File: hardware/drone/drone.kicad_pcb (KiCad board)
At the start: 4 copper layers, 70 parts, among them IC101 TPS63000IDRCRQ1, J101 1769, J103 Conn_01x05_Pin, Q103 IRLML6402TRPBF, Q104 IRLML6402TRPBF, U102 ESP32-S3, Y101 FH4000074Z

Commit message: done but need to add stitching vias
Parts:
- moved LED105 6.66 mm to (175.5, 75.5)
- moved LED106 6.66 mm to (175.6, 77.5)
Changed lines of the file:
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@@
 	(footprint "SamacSys_Parts:LEDM2214X140N"
 		(layer "F.Cu")
-		(at 181.5 80.5)
+		(at 175.55 77.5)
 		(descr "LS M67K-J2L1-1-Z")
 		(tags "LED")
@@
 	(footprint "SamacSys_Parts:LEDM2214X140N"
 		(layer "F.Cu")
-		(at 181.45 78.5)
+		(at 175.5 75.5)
 		(descr "LS M67K-J2L1-1-Z")
 		(tags "LED")

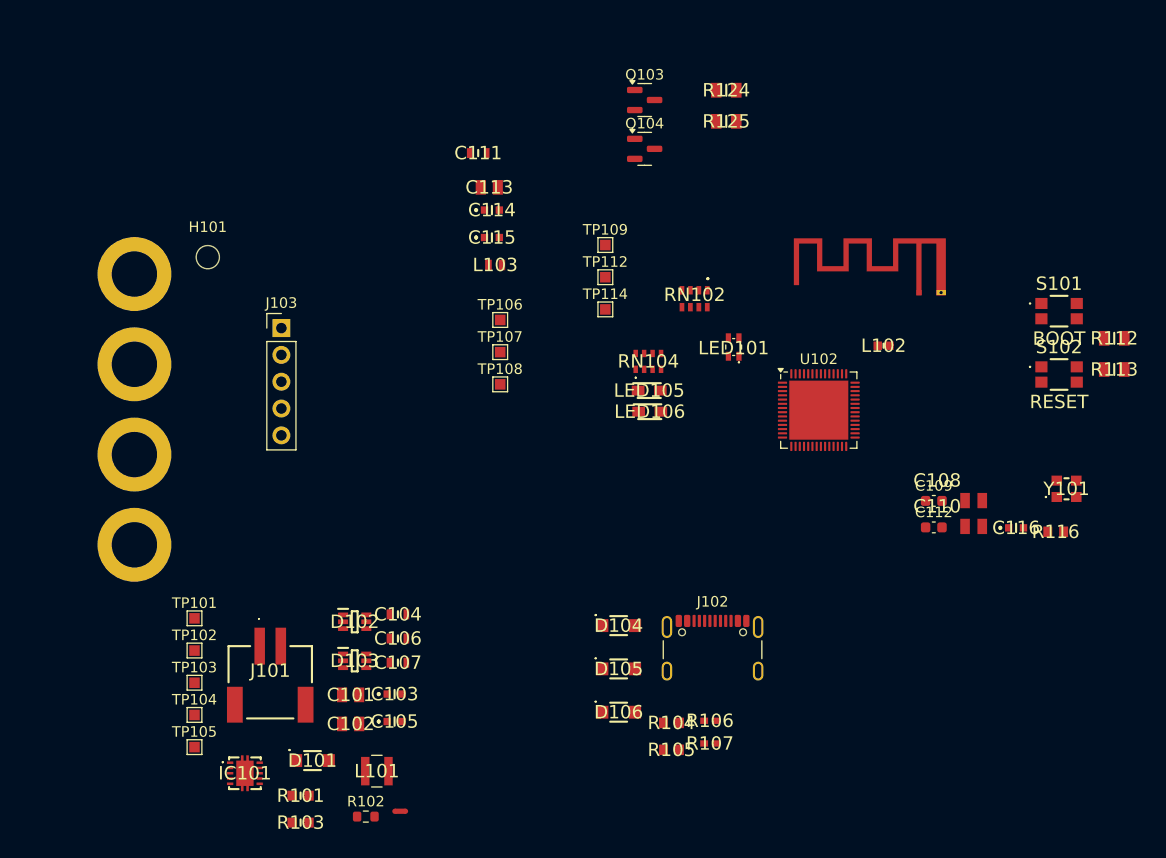
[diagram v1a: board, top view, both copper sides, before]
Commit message: save before axing motor driver ic's
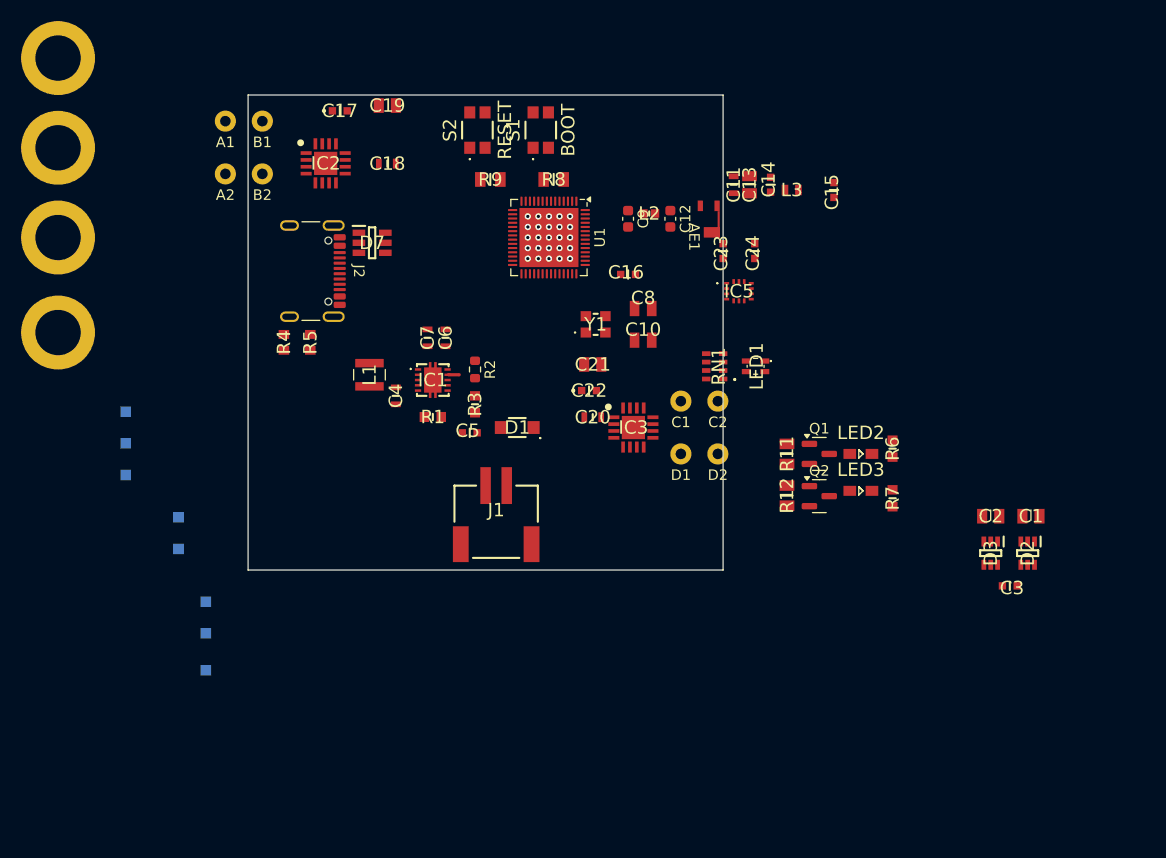
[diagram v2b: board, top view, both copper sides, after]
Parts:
- removed AE101: Antenna_Chip, SamacSys_Parts:Texas_SWRA117D_2.4GHz_Left
- removed C101, C102, C113: 1u, SamacSys_Parts:CAPC2012X135N
- removed C103, C105, C114, C115, C116: u1, SamacSys_Parts:MAJx16
- removed C104, C106, C107, C111: 10u, SamacSys_Parts:CAPC1608X80N
- removed C108, C110: 10p, SamacSys_Parts:CAPC2013X94N
- removed C109, C112: 1p8, Capacitor_SMD:C_0603_1608Metric
- removed D101, D104, D105, D106: SMF5.0A_R1_00001, SamacSys_Parts:SMF50A_R1_00001
- removed D102, D103: LM66100DCKR, SamacSys_Parts:SOP65P210X110-6N
- removed H101: MountingHole, MountingHole:MountingHole_2.2mm_M2_DIN965
- removed H102, H103, H104, H105: MountingHole_Pad, SamacSys_Parts:MountingHole_4.3mm_M4_ISO14580_Pad
- removed IC101: TPS63000IDRCRQ1, SamacSys_Parts:TPS63000IDRCRQ1
- removed J101: 1769, SamacSys_Parts:1769
- removed J102: ~, SamacSys_Parts:USB_C_Receptacle_GCT_USB4105-xx-A_16P_TopMnt_Horizontal
- removed J103: Conn_01x05_Pin, Connector_PinHeader_2.54mm:PinHeader_1x05_P2.54mm_Vertical
- removed L101: 2u2, SamacSys_Parts:NRS3015T2R2MNGHV
- removed L102: 3nH, SamacSys_Parts:INDC1006X65N
- removed L103: 2nH, SamacSys_Parts:WE-KI_0603A30
- removed LED101: SM0605RGB, SamacSys_Parts:SM0605RGB
- removed LED105, LED106: LO_M676-Q2S1-24-Z, SamacSys_Parts:LEDM2214X140N
- removed NT101: NetTie, NetTie:NetTie-2_SMD_Pad0.5mm
- removed Q103, Q104: IRLML6402TRPBF, Package_TO_SOT_SMD:SOT-23
- removed R101: 100, SamacSys_Parts:RESC1608X55N
- removed R102: 1M, Resistor_SMD:R_0603_1608Metric
- removed R103: 200k, SamacSys_Parts:RESC1608X55N
- removed R104, R105: 5k1, SamacSys_Parts:RESC1608X50N
- removed R106, R107: 27, SamacSys_Parts:RESC1005X40N
- removed R112, R113, R124, R125: 10k, SamacSys_Parts:RESC2012X60N
- removed R116: 0, SamacSys_Parts:RESC1608X50N
- removed RN102: 100 Ohms, SamacSys_Parts:EXBU38
- removed RN104: 150 Ohms, SamacSys_Parts:EXBV8V151JV
- removed S101: BOOT, SamacSys_Parts:TL1030AF500AQJ
- removed S102: RESET, SamacSys_Parts:TL1030AF500AQJ
- removed TP101: USBV, TestPoint:TestPoint_Pad_1.0x1.0mm
- removed TP102: BATV, TestPoint:TestPoint_Pad_1.0x1.0mm
- removed TP103: BUCK_VIN, TestPoint:TestPoint_Pad_1.0x1.0mm
- removed TP104: GND, TestPoint:TestPoint_Pad_1.0x1.0mm
- removed TP105: 3v3, TestPoint:TestPoint_Pad_1.0x1.0mm
- removed TP106, TP109: R, TestPoint:TestPoint_Pad_1.0x1.0mm
- removed TP107, TP112: G, TestPoint:TestPoint_Pad_1.0x1.0mm
- removed TP108, TP114: B, TestPoint:TestPoint_Pad_1.0x1.0mm
- removed U102: ESP32-S3, Package_DFN_QFN:QFN-56-1EP_7x7mm_P0.4mm_EP5.6x5.6mm
- removed Y101: FH4000074Z, SamacSys_Parts:FH4000074Z
- added AE1: Antenna_Chip, SamacSys_Parts:AANI-CH-0133, F.Cu at (180.5, 60.0)
- added C1: 1u, SamacSys_Parts:CAPC2012X135N, F.Cu at (211.7, 87.4)
- added C10: 10p, SamacSys_Parts:CAPC2013X94N, F.Cu at (174.9, 70.7)
- added C11: 10u, SamacSys_Parts:CAPC1608X80N, F.Cu at (183.5, 56.0)
- added C12: 1p8, Capacitor_SMD:C_0603_1608Metric, F.Cu at (177.5, 59.2)
- added C13: 1u, SamacSys_Parts:CAPC2012X135N, F.Cu at (185.0, 56.0)
- added C14: u1, SamacSys_Parts:MAJx16, F.Cu at (187.0, 56.0)
- added C15: u1, SamacSys_Parts:MAJx16, F.Cu at (193.0, 56.5)
- added C16: u1, SamacSys_Parts:MAJx16, F.Cu at (173.5, 64.5)
- added C17: 2u2, SamacSys_Parts:MBASx168, F.Cu at (146.2, 49.0)
- added C18: 10u, SamacSys_Parts:CAPC1608X80N, F.Cu at (150.7, 54.0)
- added C19: 10n, SamacSys_Parts:CAPC2012X90N, F.Cu at (150.7, 48.5)
- added C2: 1u, SamacSys_Parts:CAPC2012X135N, F.Cu at (207.8, 87.4)
- added C20: 10u, SamacSys_Parts:CAPC1608X80N, F.Cu at (170.2, 78.0)
- added C21: 10n, SamacSys_Parts:CAPC2012X90N, F.Cu at (170.2, 73.0)
- added C22: 2u2, SamacSys_Parts:MBASx168, F.Cu at (169.8, 75.5)
- added C23: u1, SamacSys_Parts:MAJx16, F.Cu at (182.5, 62.3)
- added C24: u1, SamacSys_Parts:MAJx16, F.Cu at (185.5, 62.3)
- added C3: u1, SamacSys_Parts:MAJx16, F.Cu at (209.7, 94.0)
- added C4: 10u, SamacSys_Parts:CAPC1608X80N, F.Cu at (151.5, 76.0)
- added C5: u1, SamacSys_Parts:MAJx16, F.Cu at (158.5, 79.5)
- added C6: 10u, SamacSys_Parts:CAPC1608X80N, F.Cu at (156.2, 70.5)
- added C7: 10u, SamacSys_Parts:CAPC1608X80N, F.Cu at (154.5, 70.5)
- added C8: 10p, SamacSys_Parts:CAPC2013X94N, F.Cu at (174.9, 67.7)
- added C9: 1p8, Capacitor_SMD:C_0603_1608Metric, F.Cu at (173.5, 59.2)
- added D1: SMF5.0A_R1_00001, SamacSys_Parts:SMF50A_R1_00001, F.Cu at (163.0, 79.0)
- added D2: LM66100DCKR, SamacSys_Parts:SOP65P210X110-6N, F.Cu at (211.3, 90.9)
- added D3: LM66100DCKR, SamacSys_Parts:SOP65P210X110-6N, F.Cu at (207.8, 90.9)
- added D7: USBLC6-4SC6Y, SamacSys_Parts:SOT95P280X145-6N, F.Cu at (149.2, 61.5)
- added H2: MountingHole_Pad, SamacSys_Parts:MountingHole_4.3mm_M4_ISO14580_Pad, F.Cu at (119.5, 44.0)
- added H3: MountingHole_Pad, SamacSys_Parts:MountingHole_4.3mm_M4_ISO14580_Pad, F.Cu at (119.5, 52.5)
- added H4: MountingHole_Pad, SamacSys_Parts:MountingHole_4.3mm_M4_ISO14580_Pad, F.Cu at (119.5, 61.0)
- added H5: MountingHole_Pad, SamacSys_Parts:MountingHole_4.3mm_M4_ISO14580_Pad, F.Cu at (119.5, 70.0)
- added IC1: TPS63000IDRCRQ1, SamacSys_Parts:TPS63000IDRCRQ1, F.Cu at (155.0, 74.5)
- added IC2: DRV8833RTYR, SamacSys_Parts:QFN65P400X400X80-17N-D, F.Cu at (144.8, 54.0)
- added IC3: DRV8833RTYR, SamacSys_Parts:QFN65P400X400X80-17N-D, F.Cu at (174.0, 79.0)
- added IC5: BMI323, SamacSys_Parts:BMI323, F.Cu at (184.0, 66.1)
- added J1: 1769, SamacSys_Parts:1769, F.Cu at (161.0, 84.5)
- added J2: ~, SamacSys_Parts:USB_C_Receptacle_GCT_USB4105-xx-A_16P_TopMnt_Horizontal, F.Cu at (142.5, 64.2)
- added L1: 2u2, SamacSys_Parts:NRS3015T2R2MNGHV, F.Cu at (149.0, 74.0)
- added L2: 3nH, SamacSys_Parts:INDC1006X65N, F.Cu at (175.5, 58.7)
- added L3: 2nH, SamacSys_Parts:WE-KI_0603A30, F.Cu at (189.0, 56.5)
- added LED1: SM0605RGB, SamacSys_Parts:SM0605RGB, F.Cu at (185.6, 73.2)
- added LED2: LO_M676-Q2S1-24-Z, SamacSys_Parts:LEDM2214X140N, F.Cu at (195.6, 81.5)
- added LED3: LO_M676-Q2S1-24-Z, SamacSys_Parts:LEDM2214X140N, F.Cu at (195.6, 85.0)
- added NT1: NetTie, SamacSys_Parts:custom_net_tie, F.Cu at (157.0, 74.0)
- added Q1: IRLML6402TRPBF, Package_TO_SOT_SMD:SOT-23, F.Cu at (191.6, 81.5)
- added Q2: IRLML6402TRPBF, Package_TO_SOT_SMD:SOT-23, F.Cu at (191.6, 85.5)
- added R1: 100, SamacSys_Parts:RESC1608X55N, F.Cu at (155.0, 78.0)
- added R11: 10k, SamacSys_Parts:RESC2012X60N, F.Cu at (188.6, 81.5)
- added R12: 10k, SamacSys_Parts:RESC2012X60N, F.Cu at (188.6, 85.5)
- added R2: 1M, Resistor_SMD:R_0603_1608Metric, F.Cu at (159.0, 73.5)
- added R3: 200k, SamacSys_Parts:RESC1608X55N, F.Cu at (159.0, 76.8)
- added R4: 5k1, SamacSys_Parts:RESC1608X50N, F.Cu at (140.9, 70.9)
- added R5: 5k1, SamacSys_Parts:RESC1608X50N, F.Cu at (143.4, 70.9)
- added R6: 100, SamacSys_Parts:RESC1608X55N, F.Cu at (198.6, 81.0)
- added R7: 100, SamacSys_Parts:RESC1608X55N, F.Cu at (198.6, 85.7)
- added R8: 10k, SamacSys_Parts:RESC2012X60N, F.Cu at (166.4, 55.5)
- added R9: 10k, SamacSys_Parts:RESC2012X60N, F.Cu at (160.4, 55.5)
- added RN1: 100 Ohms, SamacSys_Parts:EXBU38, F.Cu at (181.7, 73.2)
- added S1: BOOT, SamacSys_Parts:TL1030AF500AQJ, F.Cu at (165.2, 50.8)
- added S2: RESET, SamacSys_Parts:TL1030AF500AQJ, F.Cu at (159.2, 50.8)
- added TP1: USBV_TP, SamacSys_Parts:TestPoint_Pad_1.0x1.0mm, B.Cu at (133.5, 95.5)
- added TP10: A2, SamacSys_Parts:Motor solder point, F.Cu at (135.3, 55.0)
- added TP11: B1, SamacSys_Parts:Motor solder point, F.Cu at (138.8, 50.0)
- added TP12: B2, SamacSys_Parts:Motor solder point, F.Cu at (138.8, 55.0)
- added TP13: C1, SamacSys_Parts:Motor solder point, F.Cu at (178.5, 76.5)
- added TP14: D1, SamacSys_Parts:Motor solder point, F.Cu at (178.5, 81.5)
- added TP15: C2, SamacSys_Parts:Motor solder point, F.Cu at (182.0, 76.5)
- added TP16: D2, SamacSys_Parts:Motor solder point, F.Cu at (182.0, 81.5)
- added TP2: BATV_TP, SamacSys_Parts:TestPoint_Pad_1.0x1.0mm, B.Cu at (133.5, 98.5)
- added TP3: BUCK_VIN_TP, SamacSys_Parts:TestPoint_Pad_1.0x1.0mm, B.Cu at (133.5, 102.0)
- added TP4: GND_TP, SamacSys_Parts:TestPoint_Pad_1.0x1.0mm, B.Cu at (130.9, 87.5)
- added TP5: 3V3_TP, SamacSys_Parts:TestPoint_Pad_1.0x1.0mm, B.Cu at (130.9, 90.5)
- added TP6: R_TP, SamacSys_Parts:TestPoint_Pad_1.0x1.0mm, B.Cu at (125.9, 77.5)
- added TP7: G_TP, SamacSys_Parts:TestPoint_Pad_1.0x1.0mm, B.Cu at (125.9, 80.5)
- added TP8: B_TP, SamacSys_Parts:TestPoint_Pad_1.0x1.0mm, B.Cu at (125.9, 83.5)
- added TP9: A1, SamacSys_Parts:Motor solder point, F.Cu at (135.3, 50.0)
- added U1: ESP32-S3, Package_DFN_QFN:QFN-56-1EP_7x7mm_P0.4mm_EP5.6x5.6mm, F.Cu at (166.0, 61.0)
- added Y1: FH4000074Z, SamacSys_Parts:FH4000074Z, F.Cu at (170.4, 69.2)
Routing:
- net GND: vias 0 -> 25
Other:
- board outline added: 45 x 45 mm

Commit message: axed motor drivers. finished layout for drone but need to review overall system design after reading some stuff
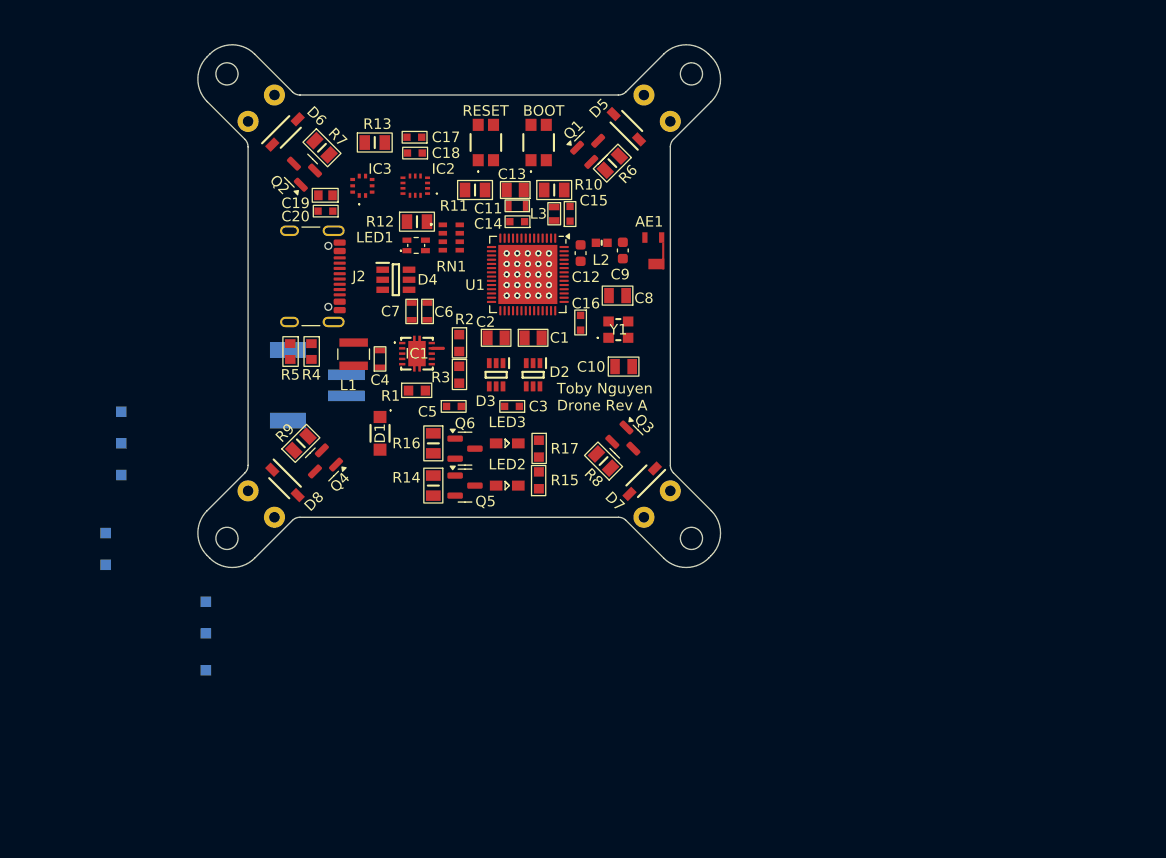
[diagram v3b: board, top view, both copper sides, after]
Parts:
- removed the C17 at (146.2, 49.0)
- removed the C18 at (150.7, 54.0)
- removed C21: 10n, SamacSys_Parts:CAPC2012X90N
- removed C22: 2u2, SamacSys_Parts:MBASx168
- removed H5: MountingHole_Pad, SamacSys_Parts:MountingHole_4.3mm_M4_ISO14580_Pad
- removed the IC2 at (144.8, 54.0)
- removed the TP14 at (178.5, 81.5)
- removed the TP15 at (182.0, 76.5)
- removed the TP16 at (182.0, 81.5)
- added D5: 1N4148WQ-7-F, SamacSys_Parts:SOD3716X145N, F.Cu at (173.3, 50.5)
- added D6: 1N4148WQ-7-F, SamacSys_Parts:SOD3716X145N, F.Cu at (141.0, 51.0)
- added D7: 1N4148WQ-7-F, SamacSys_Parts:SOD3716X145N, F.Cu at (174.8, 84.1)
- added D8: 1N4148WQ-7-F, SamacSys_Parts:SOD3716X145N, F.Cu at (141.0, 84.2)
- added H1: MountingHole, MountingHole:MountingHole_2.1mm, F.Cu at (179.5, 45.5)
- added Q1: IRLML6344, Package_TO_SOT_SMD:SOT-23, F.Cu at (170.0, 52.5)
- added Q2: IRLML6344, Package_TO_SOT_SMD:SOT-23, F.Cu at (142.5, 54.7)
- added Q3: IRLML6344, Package_TO_SOT_SMD:SOT-23, F.Cu at (173.3, 80.3)
- added Q4: IRLML6344, Package_TO_SOT_SMD:SOT-23, F.Cu at (144.5, 82.5)
- added R12: 10k, SamacSys_Parts:RESC2012X60N, F.Cu at (153.5, 59.5)
- added R13: 10k, SamacSys_Parts:RESC2012X60N, F.Cu at (149.5, 52.0)
- added R6: 10k, SamacSys_Parts:RESC2012X60N, F.Cu at (172.0, 54.0)
- added R7: 10k, SamacSys_Parts:RESC2012X60N, F.Cu at (144.5, 52.5)
- added R8: 10k, SamacSys_Parts:RESC2012X60N, F.Cu at (171.2, 82.2)
- added R9: 10k, SamacSys_Parts:RESC2012X60N, F.Cu at (142.5, 80.5)
- added TP6: A-, SamacSys_Parts:Motor solder point, F.Cu at (175.0, 47.5)
- added TP7: A+, SamacSys_Parts:Motor solder point, F.Cu at (177.5, 50.0)
- added TP8: B-, SamacSys_Parts:Motor solder point, F.Cu at (140.0, 47.5)
- C19: value 10n -> 4u7; footprint SamacSys_Parts:CAPC2012X90N -> SamacSys_Parts:CAPC1608X90N
- C20: value 10u -> u1; footprint SamacSys_Parts:CAPC1608X80N -> SamacSys_Parts:MAJx16
- H2, H3, H4: value MountingHole_Pad -> MountingHole; footprint SamacSys_Parts:MountingHole_4.3mm_M4_ISO14580_Pad -> MountingHole:MountingHole_2.1mm
- IC3: value DRV8833RTYR -> LPS25HBTR; footprint SamacSys_Parts:QFN65P400X400X80-17N-D -> SamacSys_Parts:LPS25HBTR
- J1: moved to B.Cu
- R2: footprint Resistor_SMD:R_0603_1608Metric -> SamacSys_Parts:RESC1608X55N
- TP10: value A2 -> C-
- TP11: value B1 -> C+
- TP12: value B2 -> D-
- TP13: value C1 -> D+
- TP9: value A1 -> B+
- moved H4 66.4 mm to (179.5, 89.5)
- moved TP11 52.2 mm to (177.5, 85.0)
- moved TP10 51.3 mm to (175.0, 87.5)
- moved C3 50.1 mm to (162.5, 77.0)
- moved C1 50.1 mm to (164.5, 70.5), turned to 0 degrees
- moved C2 49.8 mm to (161.0, 70.5), turned to 0 degrees
- moved D2 49.8 mm to (164.5, 74.0)
- moved D3 49.8 mm to (161.0, 74.0)
- moved TP13 41.9 mm to (137.5, 85.0)
- moved H3 40.3 mm to (135.5, 89.5)
- moved IC3 34.4 mm to (148.3, 56.1), turned to 90 degrees
- moved LED1 34.1 mm to (153.4, 61.8), turned to -90 degrees
- moved R16 33.9 mm to (155.1, 80.5)
- moved Q6 33.9 mm to (158.1, 81.0)
- moved R17 33.8 mm to (165.1, 81.0)
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- renumbered C23 to C17, C24 to C18, D7 to D4, IC5 to IC2, Q1 to Q5, Q2 to Q6, R8 to R10, R9 to R11, R11 to R14, R6 to R15, R12 to R16, R7 to R17, TP4 to TP1, TP6 to TP14, TP7 to TP15, TP8 to TP16, TP5 to TP2, TP1 to TP3, TP2 to TP4, TP3 to TP5
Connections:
- net /ESP32/INT1 renamed /ESP32/IMU.INT1
- net /ESP32/INT2 renamed /ESP32/IMU.INT2
- C16 pad 2: Net-(U1-VDD3P3_CPU) -> GND
- C19 pad 1: +BATT -> +3V3
- C19 pad 2: Net-(IC2-VCP) -> GND
- C20 pad 1: +BATT -> +3V3
- IC3 pad 1: GND -> +3V3
- IC3 pad 10: +BATT -> +3V3
- IC3 pad 2: /MOTORS/C2 -> /ESP32/SPI.SCK
- IC3 pad 3: /MOTORS/D2 -> GND
- IC3 pad 4: GND -> /ESP32/SPI.MOSI
- IC3 pad 5: /MOTORS/D1 -> /ESP32/SPI.MISO
- IC3 pad 6: /MOTORS/NFAULT2 -> /ESP32/BARO.CS
- IC3 pad 7: /ESP32/MD.DIN1 -> /ESP32/BARO.INT
- IC3 pad 8: /ESP32/MD.DIN2 -> GND
- IC3 pad 9: Net-(IC3-VCP) -> GND
- RN1 pad 5: unconnected-(RN1-Pad5) -> /ESP32/RGB.B
- RN1 pad 6: /ESP32/RGB.B -> /ESP32/RGB.G
- RN1 pad 7: /ESP32/RGB.G -> /ESP32/RGB.R
- RN1 pad 8: /ESP32/RGB.R -> unconnected-(RN1-Pad8)
- TP10 pad 1: /MOTORS/A2 -> Net-(D7-A)
- TP11 pad 1: /MOTORS/B1 -> +BATT
- TP12 pad 1: /MOTORS/B2 -> Net-(D8-A)
- TP13 pad 1: /MOTORS/C1 -> +BATT
- TP9 pad 1: /MOTORS/A1 -> +BATT
- U1 pad 10: /ESP32/MD.BIN1 -> unconnected-(U1-GPIO5/ADC1_CH4-Pad10)
- U1 pad 11: /ESP32/MD.BIN2 -> unconnected-(U1-GPIO6/ADC1_CH5-Pad11)
- U1 pad 12: /ESP32/MD.CIN1 -> unconnected-(U1-GPIO7/ADC1_CH6-Pad12)
- U1 pad 13: /ESP32/MD.CIN2 -> unconnected-(U1-GPIO8/ADC1_CH7-Pad13)
- U1 pad 14: /ESP32/MD.DIN1 -> unconnected-(U1-GPIO9/ADC1_CH8-Pad14)
- U1 pad 15: /ESP32/MD.DIN2 -> unconnected-(U1-GPIO10/ADC1_CH9-Pad15)
- U1 pad 27: /ESP32/NFAULT1 -> unconnected-(U1-GPIO21-Pad27)
- U1 pad 36: unconnected-(U1-SPICLK_N/GPIO48-Pad36) -> /ESP32/BARO.CS
- U1 pad 37: unconnected-(U1-SPICLK_P/GPIO47-Pad37) -> /ESP32/BARO.INT
- U1 pad 39: unconnected-(U1-GPIO34-Pad39) -> /ESP32/RGB.R
- U1 pad 40: unconnected-(U1-GPIO35-Pad40) -> /ESP32/RGB.G
- U1 pad 41: unconnected-(U1-GPIO36-Pad41) -> /ESP32/RGB.B
- U1 pad 43: /ESP32/NFAULT2 -> unconnected-(U1-GPIO38-Pad43)
- U1 pad 46: Net-(U1-VDD3P3_CPU) -> +3V3
- U1 pad 6: unconnected-(U1-GPIO1/ADC1_CH0-Pad6) -> /ESP32/MOTORS.MA
- U1 pad 7: /ESP32/MD.AIN1 -> /ESP32/MOTORS.MB
- U1 pad 8: unconnected-(U1-GPIO3/ADC1_CH2-Pad8) -> /ESP32/MOTORS.MC
- U1 pad 9: /ESP32/MD.AIN2 -> /ESP32/MOTORS.MD
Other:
- board size 45 x 45 mm -> 49.5 x 49.5 mm
- board text added: "Toby Nguyen Drone Rev A"
